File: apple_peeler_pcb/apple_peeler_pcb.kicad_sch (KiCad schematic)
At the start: 14 parts, among them J1 BM03B-SRSS-TB, J2 BM03B-SRSS-TB, SW1 SPST BTN, SW2 SPST BTN, U1 W25Q16JVSS, U2 RP2040, Y1 12MHz

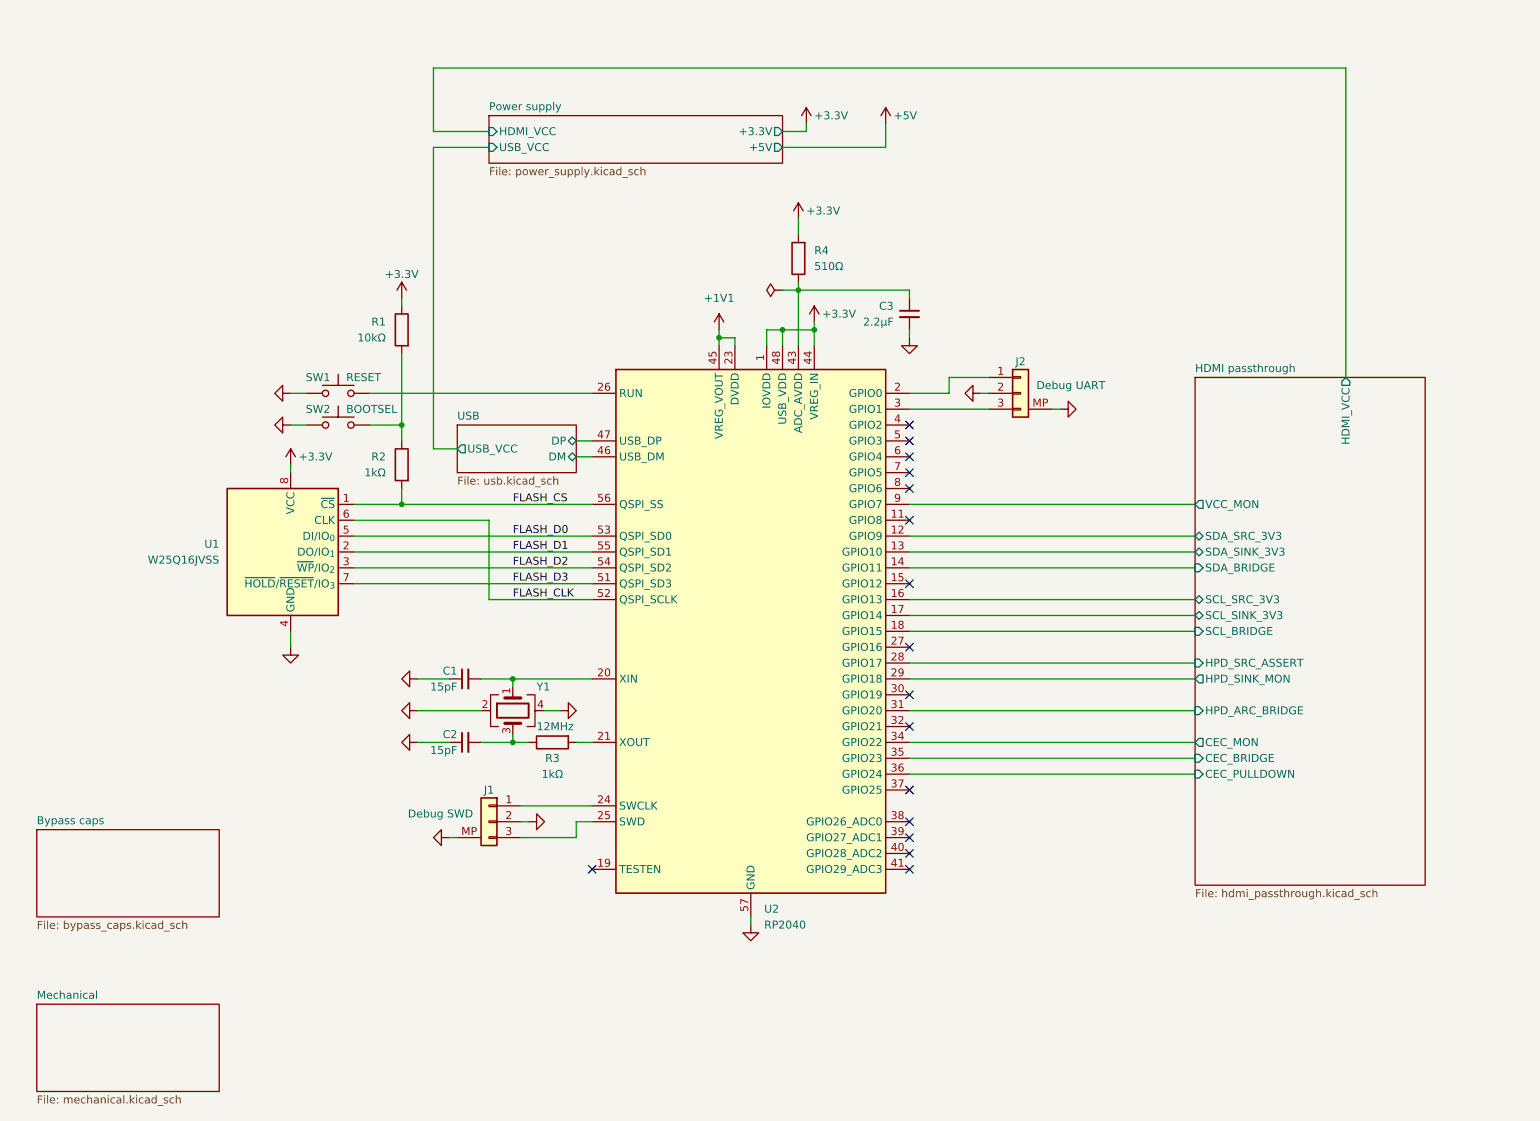
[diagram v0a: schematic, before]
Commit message: add some leds
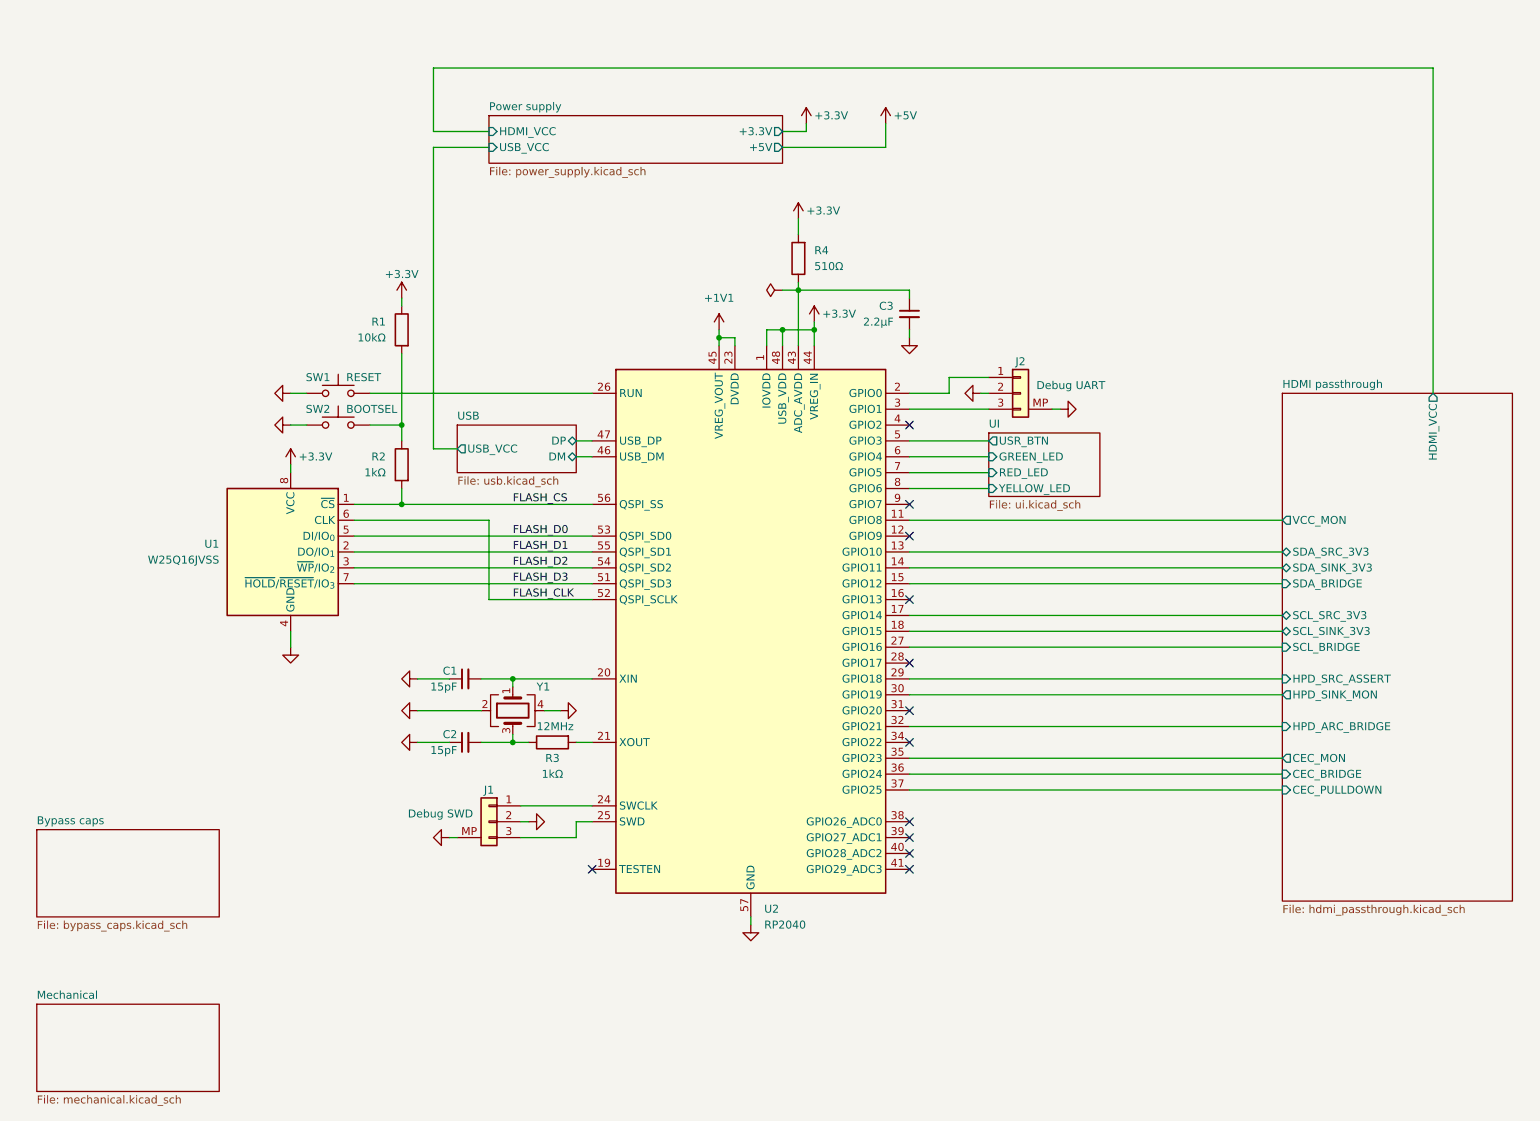
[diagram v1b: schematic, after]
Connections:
- net HDMI passthrough/CEC_BRIDGE: now also U2.36 (GPIO24); no longer U2.35 (GPIO23)
- net HDMI passthrough/CEC_MON: now also U2.35 (GPIO23); no longer U2.34 (GPIO22)
- net HDMI passthrough/CEC_PULLDOWN: now also U2.37 (GPIO25); no longer U2.36 (GPIO24)
- net HDMI passthrough/HPD_ARC_BRIDGE: now also U2.32 (GPIO21); no longer U2.31 (GPIO20)
- net HDMI passthrough/HPD_SINK_MON: now also U2.30 (GPIO19); no longer U2.29 (GPIO18)
- net HDMI passthrough/HPD_SRC_ASSERT: now also U2.29 (GPIO18); no longer U2.28 (GPIO17)
- net HDMI passthrough/SCL_BRIDGE: now also U2.27 (GPIO16); no longer U2.18 (GPIO15)
- net HDMI passthrough/SCL_SINK_3V3: now also U2.18 (GPIO15); no longer U2.17 (GPIO14)
- net HDMI passthrough/SCL_SRC_3V3: now also U2.17 (GPIO14); no longer U2.16 (GPIO13)
- net HDMI passthrough/SDA_BRIDGE: now also U2.15 (GPIO12); no longer U2.14 (GPIO11)
- net HDMI passthrough/SDA_SINK_3V3: now also U2.14 (GPIO11); no longer U2.13 (GPIO10)
- net HDMI passthrough/SDA_SRC_3V3: now also U2.13 (GPIO10); no longer U2.12 (GPIO9)
- net HDMI passthrough/VCC_MON: now also U2.11 (GPIO8); no longer U2.9 (GPIO7)
- net UI/USR_BTN: now reaches U2.5 (GPIO3)
- net UI/GREEN_LED: now reaches U2.6 (GPIO4)
- net UI/RED_LED: now reaches U2.7 (GPIO5)
- net UI/YELLOW_LED: now reaches U2.8 (GPIO6)
- no-connect marks 16 -> 12
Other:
- added sheet UI (ui.kicad_sch)
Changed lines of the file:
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@@
 	)
 	(no_connect
-		(at 168.91 124.46)
+		(at 168.91 127)
 	)
 	(no_connect
-		(at 168.91 106.68)
-	)
-	(no_connect
-		(at 168.91 91.44)
+		(at 168.91 109.22)
 	)
 	(no_connect
@@
 	)
 	(no_connect
-		(at 168.91 81.28)
-	)
-	(no_connect
 		(at 168.91 147.32)
 	)
@@
 	)
 	(no_connect
-		(at 168.91 129.54)
+		(at 168.91 132.08)
 	)
 	(no_connect
-		(at 168.91 116.84)
+		(at 168.91 93.98)
 	)
 	(no_connect
-		(at 168.91 139.7)
+		(at 168.91 81.28)
 	)
 	(no_connect
-		(at 168.91 86.36)
+		(at 168.91 119.38)
 	)
 	(no_connect
@@
 	)
 	(no_connect
-		(at 168.91 83.82)
-	)
-	(no_connect
-		(at 168.91 96.52)
-	)
-	(no_connect
-		(at 168.91 88.9)
+		(at 168.91 99.06)
 	)
 	(wire
 		(pts
-			(xy 168.91 93.98) (xy 214.63 93.98)
+			(xy 168.91 96.52) (xy 228.6 96.52)
 		)
 		(stroke
@@
 	(wire
 		(pts
-			(xy 238.76 73.66) (xy 238.76 24.13)
+			(xy 252.73 76.2) (xy 252.73 24.13)
 		)
 		(stroke
@@
 	(wire
 		(pts
-			(xy 168.91 119.38) (xy 214.63 119.38)
+			(xy 168.91 121.92) (xy 228.6 121.92)
 		)
 		(stroke
@@
 	(wire
 		(pts
-			(xy 238.76 24.13) (xy 92.71 24.13)
+			(xy 252.73 24.13) (xy 92.71 24.13)
 		)
 		(stroke
@@
 	(wire
 		(pts
+			(xy 168.91 91.44) (xy 181.61 91.44)
+		)
+		(stroke
+			(width 0)
+			(type default)
+		)
+	)
+	(wire
+		(pts
 			(xy 80.01 96.52) (xy 101.6 96.52)
 		)
@@
 	(wire
 		(pts
-			(xy 168.91 109.22) (xy 214.63 109.22)
+			(xy 168.91 111.76) (xy 228.6 111.76)
 		)
 		(stroke
@@
 	(wire
 		(pts
-			(xy 168.91 127) (xy 214.63 127)
+			(xy 168.91 129.54) (xy 228.6 129.54)
 		)
 		(stroke
@@
 	(wire
 		(pts
+			(xy 168.91 88.9) (xy 181.61 88.9)
+		)
+		(stroke
+			(width 0)
+			(type default)
+		)
+	)
+	(wire
+		(pts
 			(xy 87.63 91.44) (xy 87.63 93.98)
 		)
@@
 	(wire
 		(pts
+			(xy 168.91 86.36) (xy 181.61 86.36)
+		)
+		(stroke
+			(width 0)
+			(type default)
+		)
+	)
+	(wire
+		(pts
 			(xy 115.57 86.36) (xy 118.11 86.36)
 		)
@@
 	(wire
 		(pts
-			(xy 168.91 104.14) (xy 214.63 104.14)
+			(xy 168.91 106.68) (xy 228.6 106.68)
 		)
 		(stroke
@@
 	(wire
 		(pts
-			(xy 168.91 137.16) (xy 214.63 137.16)
+			(xy 168.91 139.7) (xy 228.6 139.7)
 		)
 		(stroke
@@
 	(wire
 		(pts
+			(xy 168.91 83.82) (xy 181.61 83.82)
+		)
+		(stroke
+			(width 0)
+			(type default)
+		)
+	)
+	(wire
+		(pts
 			(xy 87.63 60.96) (xy 87.63 62.23)
 		)
@@
 	(wire
 		(pts
-			(xy 168.91 101.6) (xy 214.63 101.6)
+			(xy 168.91 104.14) (xy 228.6 104.14)
 		)
 		(stroke
@@
 	(wire
 		(pts
-			(xy 168.91 121.92) (xy 214.63 121.92)
+			(xy 168.91 124.46) (xy 228.6 124.46)
 		)
 		(stroke
@@
 	(wire
 		(pts
-			(xy 168.91 111.76) (xy 214.63 111.76)
+			(xy 168.91 114.3) (xy 228.6 114.3)
 		)
 		(stroke
@@
 	(wire
 		(pts
-			(xy 168.91 134.62) (xy 214.63 134.62)
+			(xy 168.91 137.16) (xy 228.6 137.16)
 		)
 		(stroke
@@
 	(wire
 		(pts
-			(xy 168.91 99.06) (xy 214.63 99.06)
+			(xy 168.91 101.6) (xy 228.6 101.6)
 		)
 		(stroke
@@
 	(wire
 		(pts
-			(xy 168.91 132.08) (xy 214.63 132.08)
+			(xy 168.91 134.62) (xy 228.6 134.62)
 		)
 		(stroke
@@
 	(wire
 		(pts
-			(xy 168.91 114.3) (xy 214.63 114.3)
+			(xy 168.91 116.84) (xy 228.6 116.84)
 		)
 		(stroke
@@
 	)
 	(sheet
-		(at 214.63 73.66)
+		(at 228.6 76.2)
 		(size 36.83 81.28)
 		(exclude_from_sim no)
@@
 		)
 		(property "Sheetname" "HDMI passthrough"
-			(at 214.63 72.9484 0)
+			(at 228.6 75.4884 0)
 			(effects
 				(font
@@
 		)
 		(property "Sheetfile" "hdmi_passthrough.kicad_sch"
-			(at 214.63 155.5246 0)
+			(at 228.6 158.0646 0)
 			(effects
 				(font
@@
 		)
 		(pin "CEC_BRIDGE" input
-			(at 214.63 134.62 180)
+			(at 228.6 137.16 180)
 			(effects
 				(font
@@
 		)
 		(pin "CEC_MON" output
-			(at 214.63 132.08 180)
+			(at 228.6 134.62 180)
 			(effects
 				(font
@@
 		)
 		(pin "CEC_PULLDOWN" input
-			(at 214.63 137.16 180)
+			(at 228.6 139.7 180)
 			(effects
 				(font
@@
 		)
 		(pin "HDMI_VCC" output
-			(at 238.76 73.66 90)
+			(at 252.73 76.2 90)
 			(effects
 				(font
@@
 		)
 		(pin "HPD_ARC_BRIDGE" input
-			(at 214.63 127 180)
+			(at 228.6 129.54 180)
 			(effects
 				(font
@@
 		)
 		(pin "HPD_SINK_MON" output
-			(at 214.63 121.92 180)
+			(at 228.6 124.46 180)
 			(effects
 				(font
@@
 		)
 		(pin "HPD_SRC_ASSERT" input
-			(at 214.63 119.38 180)
+			(at 228.6 121.92 180)
 			(effects
 				(font
@@
 		)
 		(pin "SCL_BRIDGE" input
-			(at 214.63 114.3 180)
+			(at 228.6 116.84 180)
 			(effects
 				(font
@@
 		)
 		(pin "SCL_SINK_3V3" bidirectional
-			(at 214.63 111.76 180)
+			(at 228.6 114.3 180)
 			(effects
 				(font
@@
 		)
 		(pin "SCL_SRC_3V3" bidirectional
-			(at 214.63 109.22 180)
+			(at 228.6 111.76 180)
 			(effects
 				(font
@@
 		)
 		(pin "SDA_BRIDGE" input
-			(at 214.63 104.14 180)
+			(at 228.6 106.68 180)
 			(effects
 				(font
@@
 		)
 		(pin "SDA_SINK_3V3" bidirectional
-			(at 214.63 101.6 180)
+			(at 228.6 104.14 180)
 			(effects
 				(font
@@
 		)
 		(pin "SDA_SRC_3V3" bidirectional
-			(at 214.63 99.06 180)
+			(at 228.6 101.6 180)
 			(effects
 				(font
@@
 		)
 		(pin "VCC_MON" output
-			(at 214.63 93.98 180)
+			(at 228.6 96.52 180)
 			(effects
 				(font
@@
 				)
 			)
+		)
+	)
+	(sheet
+		(at 181.61 82.55)
+		(size 17.78 10.16)
+		(exclude_from_sim no)
+		(in_bom yes)
+		(on_board yes)
+		(dnp no)
+		(fields_autoplaced yes)
+		(stroke
+			(width 0.1524)
+			(type solid)
+		)
+		(fill
+			(color 0 0 0 0.0000)
+		)
+		(property "Sheetname" "UI"
+			(at 181.61 81.8384 0)
+			(effects
+				(font
+					(size 1.27 1.27)
+				)
+				(justify left bottom)
+			)
+		)
+		(property "Sheetfile" "ui.kicad_sch"
+			(at 181.61 93.2946 0)
+			(effects
+				(font
+					(size 1.27 1.27)
+				)
+				(justify left top)
+			)
+		)
+		(pin "GREEN_LED" input
+			(at 181.61 86.36 180)
+			(effects
+				(font
+					(size 1.27 1.27)
+				)
+				(justify left)
+			)
+		)
+		(pin "RED_LED" input
+			(at 181.61 88.9 180)
+			(effects
+				(font
+					(size 1.27 1.27)
+				)
+				(justify left)
+			)
+		)
+		(pin "USR_BTN" output
+			(at 181.61 83.82 180)
+			(effects
+				(font
+					(size 1.27 1.27)
+				)
+				(justify left)
+			)
+		)
+		(pin "YELLOW_LED" input
+			(at 181.61 91.44 180)
+			(effects
+				(font
+					(size 1.27 1.27)
+				)
+				(justify left)
+			)
+		)
+		(instances
+			(project "apple_peeler_pcb"
+				(path "/d5946b96-44a8-4a28-8641-19803e1510af"
+					(page "20")
+				)
+			)

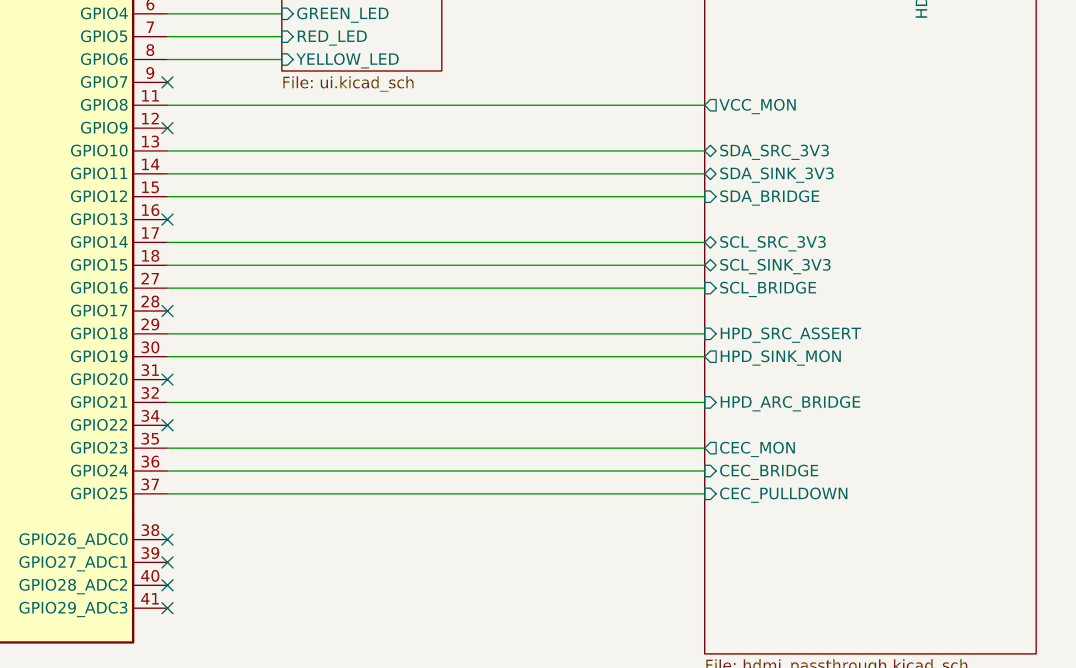
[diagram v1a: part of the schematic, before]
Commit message: we paid for all the pins, we're gonna use all the pins
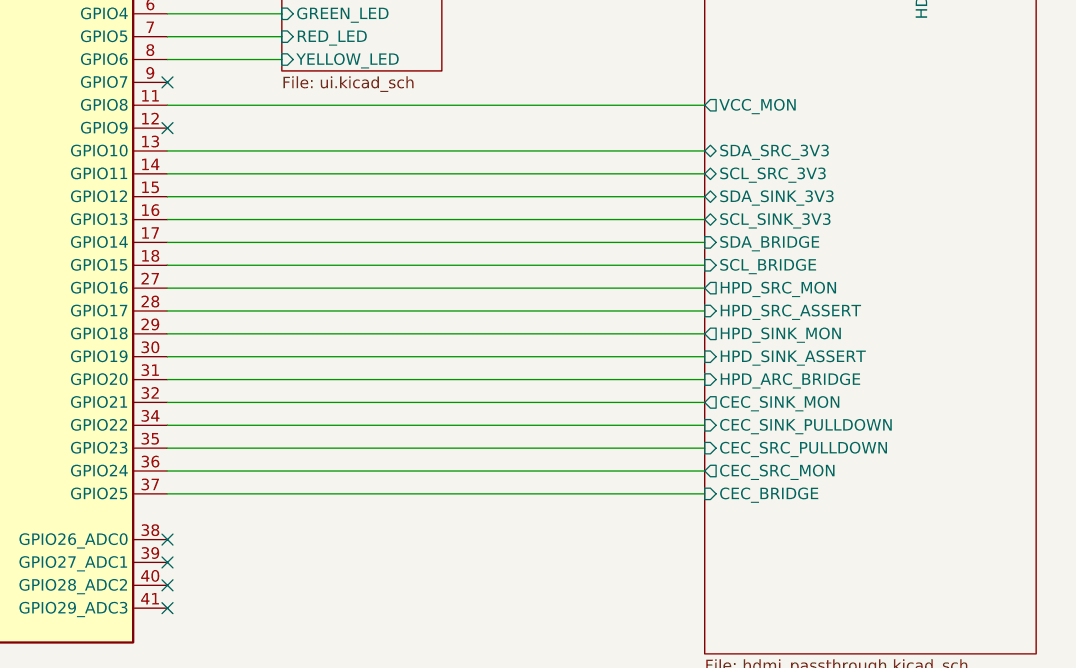
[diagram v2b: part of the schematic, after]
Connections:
- net HDMI passthrough/CEC_PULLDOWN is gone; now on net HDMI passthrough/CEC_BRIDGE: U2.37 (GPIO25)
- net HDMI passthrough/CEC_BRIDGE: no longer U2.36 (GPIO24)
- net HDMI passthrough/HPD_ARC_BRIDGE: now also U2.31 (GPIO20); no longer U2.32 (GPIO21)
- net HDMI passthrough/HPD_SINK_MON: now also U2.29 (GPIO18); no longer U2.30 (GPIO19)
- net HDMI passthrough/HPD_SRC_ASSERT: now also U2.28 (GPIO17); no longer U2.29 (GPIO18)
- net HDMI passthrough/SCL_BRIDGE: now also U2.18 (GPIO15); no longer U2.27 (GPIO16)
- net HDMI passthrough/SCL_SINK_3V3: now also U2.16 (GPIO13); no longer U2.18 (GPIO15)
- net HDMI passthrough/SCL_SRC_3V3: now also U2.14 (GPIO11); no longer U2.17 (GPIO14)
- net HDMI passthrough/SDA_BRIDGE: now also U2.17 (GPIO14); no longer U2.15 (GPIO12)
- net HDMI passthrough/SDA_SINK_3V3: now also U2.15 (GPIO12); no longer U2.14 (GPIO11)
- net HDMI passthrough/CEC_SINK_PULLDOWN: now reaches U2.34 (GPIO22)
- net HDMI passthrough/CEC_MON renamed HDMI passthrough/CEC_SRC_PULLDOWN
- new net HDMI passthrough/CEC_SINK_MON: U2.32 (GPIO21)
- new net HDMI passthrough/CEC_SRC_MON: U2.36 (GPIO24)
- new net HDMI passthrough/HPD_SINK_ASSERT: U2.30 (GPIO19)
- new net HDMI passthrough/HPD_SRC_MON: U2.27 (GPIO16)
- no-connect marks 12 -> 8
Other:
- sheet HDMI passthrough ports: added CEC_SINK_MON, CEC_SINK_PULLDOWN, CEC_SRC_MON, CEC_SRC_PULLDOWN, HPD_SINK_ASSERT, HPD_SRC_MON; removed CEC_MON, CEC_PULLDOWN
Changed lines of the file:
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@@
 	)
 	(no_connect
-		(at 168.91 127)
-	)
-	(no_connect
-		(at 168.91 109.22)
-	)
-	(no_connect
 		(at 168.91 152.4)
 	)
@@
 	)
 	(no_connect
-		(at 168.91 132.08)
-	)
-	(no_connect
 		(at 168.91 93.98)
 	)
@@
 	)
 	(no_connect
-		(at 168.91 119.38)
-	)
-	(no_connect
 		(at 118.11 152.4)
 	)
@@
 	(wire
 		(pts
+			(xy 168.91 109.22) (xy 228.6 109.22)
+		)
+		(stroke
+			(width 0)
+			(type default)
+		)
+	)
+	(wire
+		(pts
 			(xy 168.91 60.96) (xy 168.91 59.69)
 		)
@@
 	(wire
 		(pts
+			(xy 168.91 127) (xy 228.6 127)
+		)
+		(stroke
+			(width 0)
+			(type default)
+		)
+	)
+	(wire
+		(pts
 			(xy 140.97 67.31) (xy 140.97 68.58)
 		)
@@
 	(wire
 		(pts
+			(xy 168.91 119.38) (xy 228.6 119.38)
+		)
+		(stroke
+			(width 0)
+			(type default)
+		)
+	)
+	(wire
+		(pts
 			(xy 105.41 121.92) (xy 105.41 123.19)
 		)
@@
 	(wire
 		(pts
+			(xy 168.91 132.08) (xy 228.6 132.08)
+		)
+		(stroke
+			(width 0)
+			(type default)
+		)
+	)
+	(wire
+		(pts
 			(xy 82.55 76.2) (xy 118.11 76.2)
 		)
@@
 		)
 		(pin "CEC_BRIDGE" input
-			(at 228.6 137.16 180)
-			(effects
-				(font
-					(size 1.27 1.27)
-				)
-				(justify left)
-			)
-		)
-		(pin "CEC_MON" output
-			(at 228.6 134.62 180)
-			(effects
-				(font
-					(size 1.27 1.27)
-				)
-				(justify left)
-			)
-		)
-		(pin "CEC_PULLDOWN" input
 			(at 228.6 139.7 180)
 			(effects
@@
 		)
 		(pin "HPD_ARC_BRIDGE" input
-			(at 228.6 129.54 180)
+			(at 228.6 127 180)
 			(effects
 				(font
@@
 		)
 		(pin "HPD_SINK_MON" output
-			(at 228.6 124.46 180)
+			(at 228.6 121.92 180)
 			(effects
 				(font
@@
 		)
 		(pin "HPD_SRC_ASSERT" input
-			(at 228.6 121.92 180)
+			(at 228.6 119.38 180)
 			(effects
 				(font
@@
 		)
 		(pin "SCL_BRIDGE" input
-			(at 228.6 116.84 180)
+			(at 228.6 114.3 180)
 			(effects
 				(font
@@
 		)
 		(pin "SCL_SINK_3V3" bidirectional
-			(at 228.6 114.3 180)
+			(at 228.6 109.22 180)
 			(effects
 				(font
@@
 		)
 		(pin "SCL_SRC_3V3" bidirectional
-			(at 228.6 111.76 180)
+			(at 228.6 104.14 180)
 			(effects
 				(font
@@
 		)
 		(pin "SDA_BRIDGE" input
-			(at 228.6 106.68 180)
+			(at 228.6 111.76 180)
 			(effects
 				(font
@@
 		)
 		(pin "SDA_SINK_3V3" bidirectional
-			(at 228.6 104.14 180)
+			(at 228.6 106.68 180)
 			(effects
 				(font
@@
 			(effects
 				(font
+					(size 1.27 1.27)
+				)
+				(justify left)
+			)
+		)
+		(pin "CEC_SINK_MON" output
+			(at 228.6 129.54 180)
+			(effects
+				(font
+					(size 1.27 1.27)
+				)
+				(justify left)
+			)
+		)
+		(pin "CEC_SINK_PULLDOWN" input
+			(at 228.6 132.08 180)
+			(effects
+				(font
+					(size 1.27 1.27)
+				)
+				(justify left)
+			)
+		)
+		(pin "CEC_SRC_MON" output
+			(at 228.6 137.16 180)
+			(effects
+				(font
+					(size 1.27 1.27)
+				)
+				(justify left)
+			)
+		)
+		(pin "CEC_SRC_PULLDOWN" input
+			(at 228.6 134.62 180)
+			(effects
+				(font
+					(size 1.27 1.27)
+				)
+				(justify left)
+			)
+		)
+		(pin "HPD_SINK_ASSERT" input
+			(at 228.6 124.46 180)
+			(effects
+				(font
+					(size 1.27 1.27)
+				)
+				(justify left)
+			)
+		)
+		(pin "HPD_SRC_MON" output
+			(at 228.6 116.84 180)
+			(effects
+				(font
